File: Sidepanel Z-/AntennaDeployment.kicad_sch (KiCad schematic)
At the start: 5 parts, among them Q1 BSS214NW

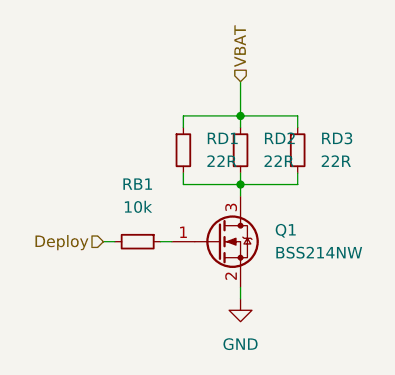
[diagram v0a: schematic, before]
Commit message: Paar Fehler behoben, Z+ no MOSFET
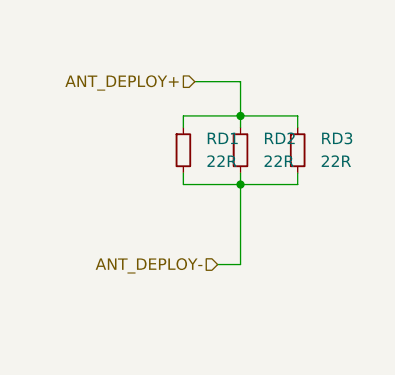
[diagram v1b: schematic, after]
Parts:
- removed Q1: BSS214NW, Package_TO_SOT_SMD:SOT-323_SC-70, symbol Transistor_FET:BSS214NW
- removed RB1: 10k, Resistor_SMD:R_0603_1608Metric, symbol Device:R_Small
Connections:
- net ANT_DEPLOY-: now reaches RD1.2, RD2.2, RD3.2
- net VBAT renamed ANT_DEPLOY+
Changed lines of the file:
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@@
     (stroke (width 0) (type default) (color 0 0 0 0))
   )
-  (wire (pts (xy 26.67 45.72) (xy 27.94 45.72))
-    (stroke (width 0) (type default) (color 0 0 0 0))
-  )
-  (wire (pts (xy 35.56 39.37) (xy 35.56 40.64))
-    (stroke (width 0) (type default) (color 0 0 0 0))
-  )
-  (wire (pts (xy 35.56 50.8) (xy 35.56 52.07))
+  (wire (pts (xy 35.56 39.37) (xy 35.56 48.26))
     (stroke (width 0) (type default) (color 0 0 0 0))
   )
   (wire (pts (xy 35.56 31.75) (xy 35.56 33.02))
+    (stroke (width 0) (type default) (color 0 0 0 0))
+  )
+  (wire (pts (xy 30.48 27.94) (xy 35.56 27.94))
     (stroke (width 0) (type default) (color 0 0 0 0))
   )
@@
   )
   (wire (pts (xy 29.21 38.1) (xy 29.21 39.37))
-    (stroke (width 0) (type default) (color 0 0 0 0))
-  )
-  (wire (pts (xy 20.32 45.72) (xy 21.59 45.72))
     (stroke (width 0) (type default) (color 0 0 0 0))
   )
@@
     (stroke (width 0) (type default) (color 0 0 0 0))
   )
+  (wire (pts (xy 35.56 48.26) (xy 33.02 48.26))
+    (stroke (width 0) (type default) (color 0 0 0 0))
+  )
   (wire (pts (xy 41.91 39.37) (xy 41.91 38.1))
     (stroke (width 0) (type default) (color 0 0 0 0))
@@
     (stroke (width 0) (type default) (color 0 0 0 0))
   )
-  (hierarchical_label "VBAT" (shape input) (at 35.56 27.94 90)
-    (effects (font (size 1.27 1.27)) (justify left))
+  (hierarchical_label "ANT_DEPLOY-" (shape input) (at 33.02 48.26 180)
+    (effects (font (size 1.27 1.27)) (justify right))
   )
-  (hierarchical_label "Deploy" (shape input) (at 20.32 45.72 180)
+  (hierarchical_label "ANT_DEPLOY+" (shape input) (at 30.48 27.94 180)
     (effects (font (size 1.27 1.27)) (justify right))
   )
@@
     (pin "1")
     (pin "2")
-  )
-  (symbol (lib_id "Device:R_Small") (at 24.13 45.72 270) (unit 1)
-    (in_bom yes) (on_board yes) (fields_autoplaced)
-    (property "Reference" "RB1" (id 0) (at 24.13 39.37 90))
-    (property "Value" "10k" (id 1) (at 24.13 41.91 90))
-    (property "Footprint" "Resistor_SMD:R_0603_1608Metric" (id 2) (at 24.13 45.72 0)
-      (effects (font (size 1.27 1.27)) hide)
-    )
-    (property "Datasheet" "~" (id 3) (at 24.13 45.72 0)
-      (effects (font (size 1.27 1.27)) hide)
-    )
-    (pin "1")
-    (pin "2")
-  )
-  (symbol (lib_id "Transistor_FET:BSS214NW") (at 33.02 45.72 0) (unit 1)
-    (in_bom yes) (on_board yes) (fields_autoplaced)
-    (property "Reference" "Q1" (id 0) (at 39.37 44.4499 0)
-      (effects (font (size 1.27 1.27)) (justify left))
-    )
-    (property "Value" "BSS214NW" (id 1) (at 39.37 46.9899 0)
-      (effects (font (size 1.27 1.27)) (justify left))
-    )
-    (property "Footprint" "Package_TO_SOT_SMD:SOT-323_SC-70" (id 2) (at 38.1 47.625 0)
-      (effects (font (size 1.27 1.27) italic) (justify left) hide)
-    )
-    (property "Datasheet" "https://www.infineon.com/dgdl/Infineon-BSS214NW-DS-v02_02-en.pdf?fileId=db3a30431b3e89eb011b695aebc01bde" (id 3) (at 33.02 45.72 0)
-      (effects (font (size 1.27 1.27)) (justify left) hide)
-    )
-    (pin "1")
-    (pin "2")
-    (pin "3")
   )
   (symbol (lib_id "Device:R_Small") (at 41.91 35.56 0) (unit 1)
@@
     (pin "2")
   )
-  (symbol (lib_id "power:GND") (at 35.56 52.07 0) (unit 1)
-    (in_bom yes) (on_board yes) (fields_autoplaced)
-    (property "Reference" "#PWR05" (id 0) (at 35.56 58.42 0)
-      (effects (font (size 1.27 1.27)) hide)
-    )
-    (property "Value" "GND" (id 1) (at 35.56 57.15 0))
-    (property "Footprint" "" (id 2) (at 35.56 52.07 0)
-      (effects (font (size 1.27 1.27)) hide)
-    )
-    (property "Datasheet" "" (id 3) (at 35.56 52.07 0)
-      (effects (font (size 1.27 1.27)) hide)
-    )
-    (pin "1")
-  )
 )

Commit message: Changed the layout of all the sidepanel PCBs to mitigate the problems that arised from the bad previous design.
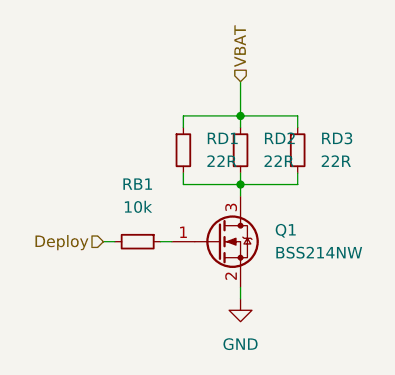
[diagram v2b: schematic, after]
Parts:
- added Q1: BSS214NW, Package_TO_SOT_SMD:SOT-323_SC-70, symbol Transistor_FET:BSS214NW
- added RB1: 10k, Resistor_SMD:R_0603_1608Metric, symbol Device:R_Small
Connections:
- net ANT_DEPLOY+ renamed VBAT
- net ANT_DEPLOY-: no longer names the net of RD1.2, RD2.2, RD3.2
- net ANT_DEPLOY-: now also Q1.3 (D)
- new net: Q1.1 (G), RB1.1
- new net Deploy: RB1.2
- new net GND: Q1.2 (S)
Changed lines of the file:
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@@
     (stroke (width 0) (type default) (color 0 0 0 0))
   )
-  (wire (pts (xy 35.56 39.37) (xy 35.56 48.26))
+  (wire (pts (xy 26.67 45.72) (xy 27.94 45.72))
+    (stroke (width 0) (type default) (color 0 0 0 0))
+  )
+  (wire (pts (xy 35.56 39.37) (xy 35.56 40.64))
+    (stroke (width 0) (type default) (color 0 0 0 0))
+  )
+  (wire (pts (xy 35.56 50.8) (xy 35.56 52.07))
     (stroke (width 0) (type default) (color 0 0 0 0))
   )
   (wire (pts (xy 35.56 31.75) (xy 35.56 33.02))
-    (stroke (width 0) (type default) (color 0 0 0 0))
-  )
-  (wire (pts (xy 30.48 27.94) (xy 35.56 27.94))
     (stroke (width 0) (type default) (color 0 0 0 0))
   )
@@
   )
   (wire (pts (xy 29.21 38.1) (xy 29.21 39.37))
+    (stroke (width 0) (type default) (color 0 0 0 0))
+  )
+  (wire (pts (xy 20.32 45.72) (xy 21.59 45.72))
     (stroke (width 0) (type default) (color 0 0 0 0))
   )
@@
     (stroke (width 0) (type default) (color 0 0 0 0))
   )
-  (wire (pts (xy 35.56 48.26) (xy 33.02 48.26))
-    (stroke (width 0) (type default) (color 0 0 0 0))
-  )
   (wire (pts (xy 41.91 39.37) (xy 41.91 38.1))
     (stroke (width 0) (type default) (color 0 0 0 0))
@@
     (stroke (width 0) (type default) (color 0 0 0 0))
   )
-  (hierarchical_label "ANT_DEPLOY-" (shape input) (at 33.02 48.26 180)
-    (effects (font (size 1.27 1.27)) (justify right))
+  (hierarchical_label "VBAT" (shape input) (at 35.56 27.94 90)
+    (effects (font (size 1.27 1.27)) (justify left))
   )
-  (hierarchical_label "ANT_DEPLOY+" (shape input) (at 30.48 27.94 180)
+  (hierarchical_label "Deploy" (shape input) (at 20.32 45.72 180)
     (effects (font (size 1.27 1.27)) (justify right))
   )
@@
     (pin "1")
     (pin "2")
+  )
+  (symbol (lib_id "Device:R_Small") (at 24.13 45.72 270) (unit 1)
+    (in_bom yes) (on_board yes) (fields_autoplaced)
+    (property "Reference" "RB1" (id 0) (at 24.13 39.37 90))
+    (property "Value" "10k" (id 1) (at 24.13 41.91 90))
+    (property "Footprint" "Resistor_SMD:R_0603_1608Metric" (id 2) (at 24.13 45.72 0)
+      (effects (font (size 1.27 1.27)) hide)
+    )
+    (property "Datasheet" "~" (id 3) (at 24.13 45.72 0)
+      (effects (font (size 1.27 1.27)) hide)
+    )
+    (pin "1")
+    (pin "2")
+  )
+  (symbol (lib_id "Transistor_FET:BSS214NW") (at 33.02 45.72 0) (unit 1)
+    (in_bom yes) (on_board yes) (fields_autoplaced)
+    (property "Reference" "Q1" (id 0) (at 39.37 44.4499 0)
+      (effects (font (size 1.27 1.27)) (justify left))
+    )
+    (property "Value" "BSS214NW" (id 1) (at 39.37 46.9899 0)
+      (effects (font (size 1.27 1.27)) (justify left))
+    )
+    (property "Footprint" "Package_TO_SOT_SMD:SOT-323_SC-70" (id 2) (at 38.1 47.625 0)
+      (effects (font (size 1.27 1.27) italic) (justify left) hide)
+    )
+    (property "Datasheet" "https://www.infineon.com/dgdl/Infineon-BSS214NW-DS-v02_02-en.pdf?fileId=db3a30431b3e89eb011b695aebc01bde" (id 3) (at 33.02 45.72 0)
+      (effects (font (size 1.27 1.27)) (justify left) hide)
+    )
+    (pin "1")
+    (pin "2")
+    (pin "3")
   )
   (symbol (lib_id "Device:R_Small") (at 41.91 35.56 0) (unit 1)
@@
     (pin "2")
   )
+  (symbol (lib_id "power:GND") (at 35.56 52.07 0) (unit 1)
+    (in_bom yes) (on_board yes) (fields_autoplaced)
+    (property "Reference" "#PWR05" (id 0) (at 35.56 58.42 0)
+      (effects (font (size 1.27 1.27)) hide)
+    )
+    (property "Value" "GND" (id 1) (at 35.56 57.15 0))
+    (property "Footprint" "" (id 2) (at 35.56 52.07 0)
+      (effects (font (size 1.27 1.27)) hide)
+    )
+    (property "Datasheet" "" (id 3) (at 35.56 52.07 0)
+      (effects (font (size 1.27 1.27)) hide)
+    )
+    (pin "1")
+  )
 )
